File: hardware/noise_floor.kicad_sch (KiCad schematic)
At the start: 15 parts, among them J1 DC Power, J10 IO/Switch Connector 2 (Switch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, J2 Input, J3 Output, J4 Battery Negative (optional), J5 Battery Positive (optional), J6 IO/Effect Connector 1 (IO Sid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, J7 IO/Switch Connector 1 (IO Sid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, J8 IO/Switch Connector 2 (IO Sid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, J9 IO/Switch Connector 1 (Switch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, SW1 Footswitch

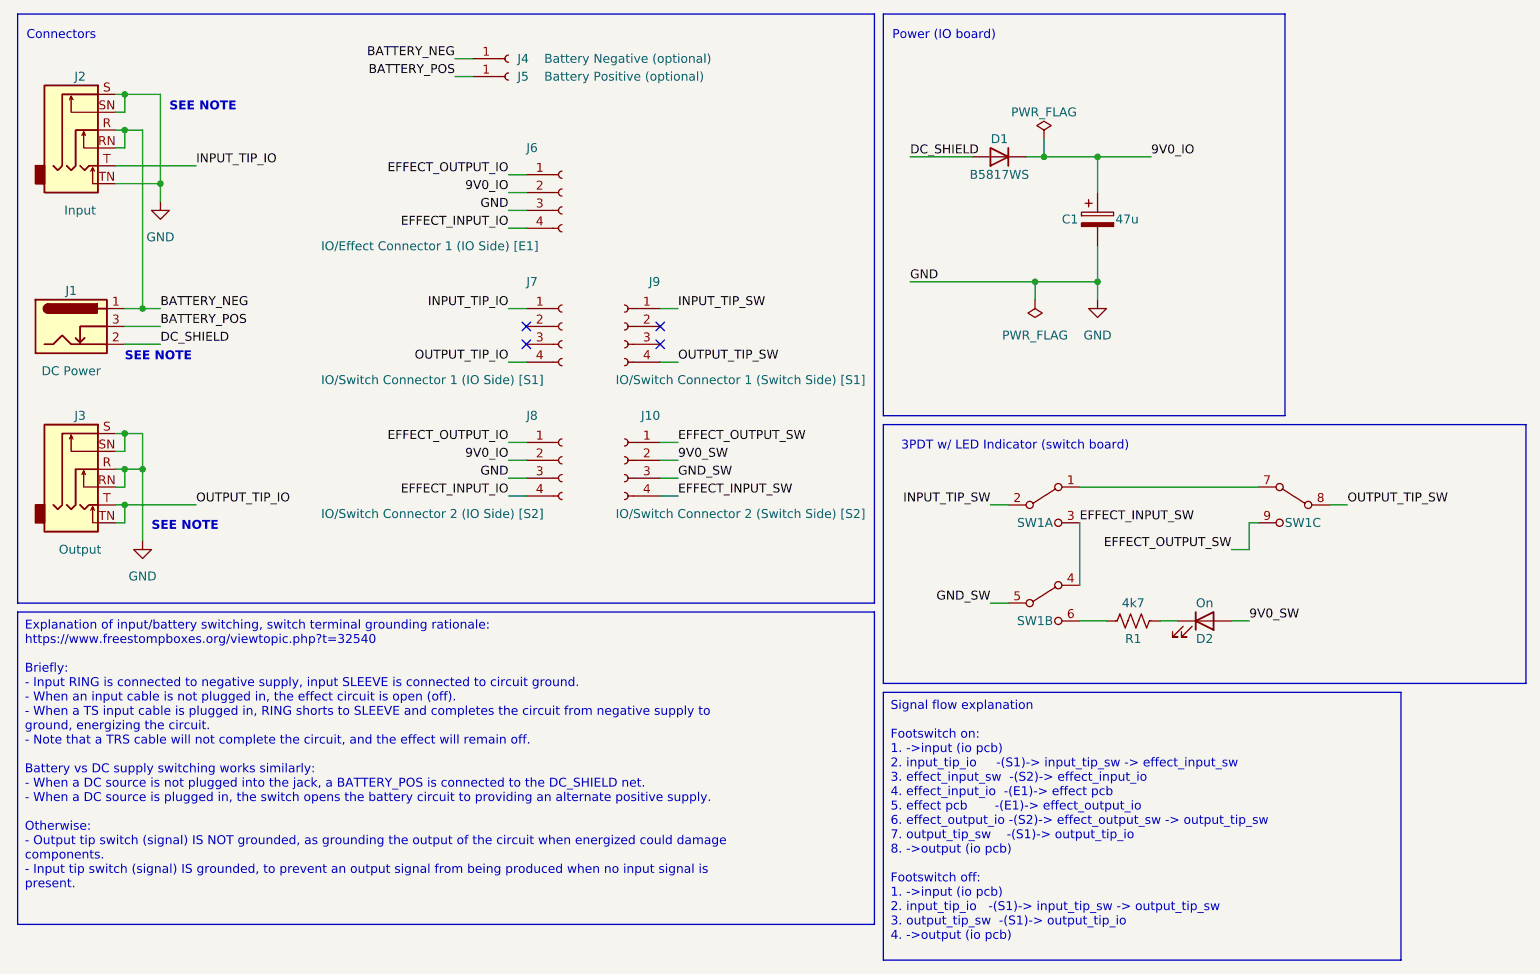
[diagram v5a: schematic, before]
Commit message: slight adjustment to input switch behavior, add note about chassis ground
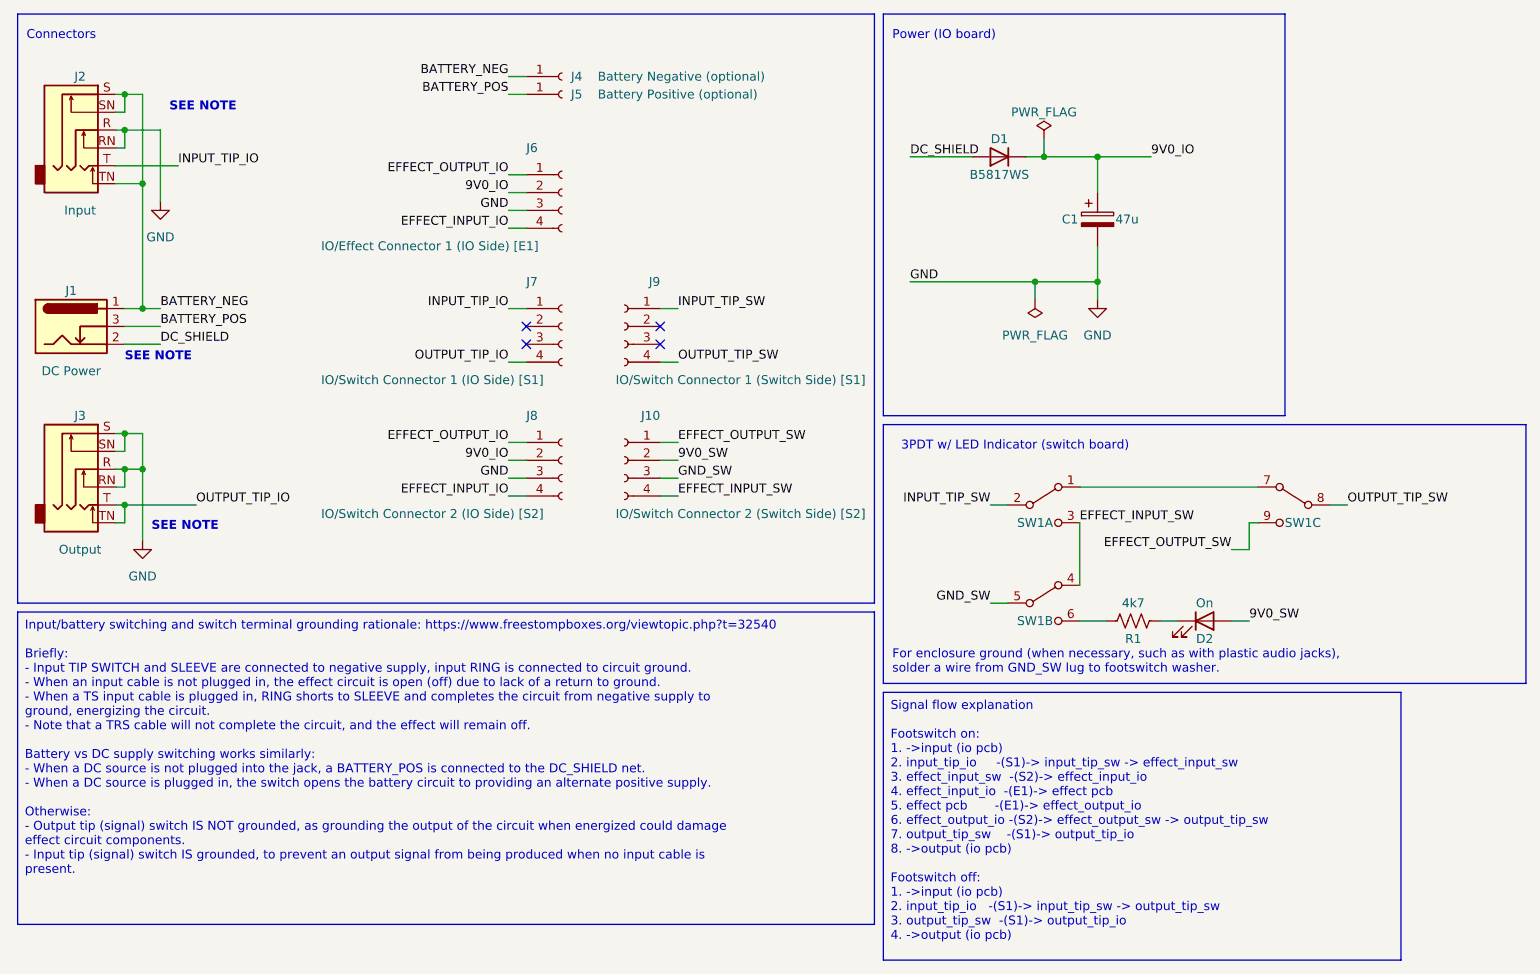
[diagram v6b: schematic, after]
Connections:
- net BATTERY_NEG: now also J2.S, J2.SN, J2.TN; no longer J2.R, J2.RN
- net GND: now also J2.R, J2.RN; no longer J2.S, J2.SN, J2.TN
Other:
- note added: "For enclosure ground (when necessary, such as with plastic audio jacks), solder a wire from GND_SW lug to footswitch washer."
- moved on the sheet: J4, J5

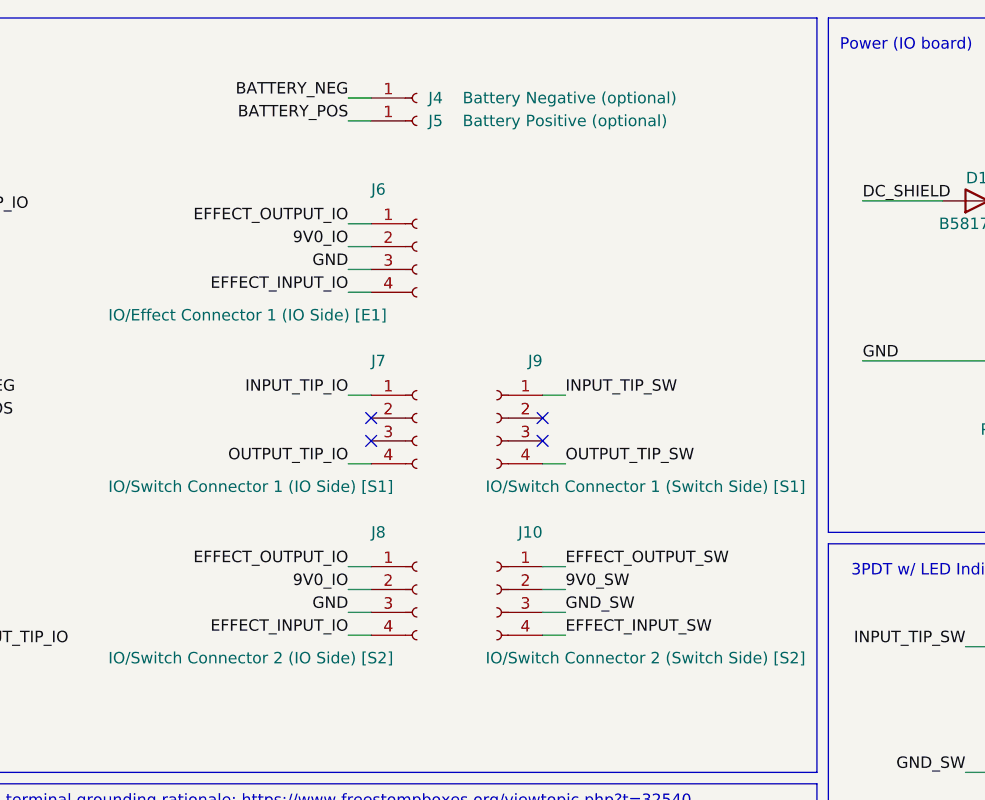
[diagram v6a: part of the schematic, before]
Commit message: Fix errata from v0.03 prototype inspection:
 - Switch to narrower amphenol phone jacks to better fit within 125B enclosure
 - Swap pin ordering for picoblade connections on IO board, as retail cable assemblies swap pin order
 -

Also:

 - Add JST XH header for battery connection

Another commit will complete the reroute shortly.
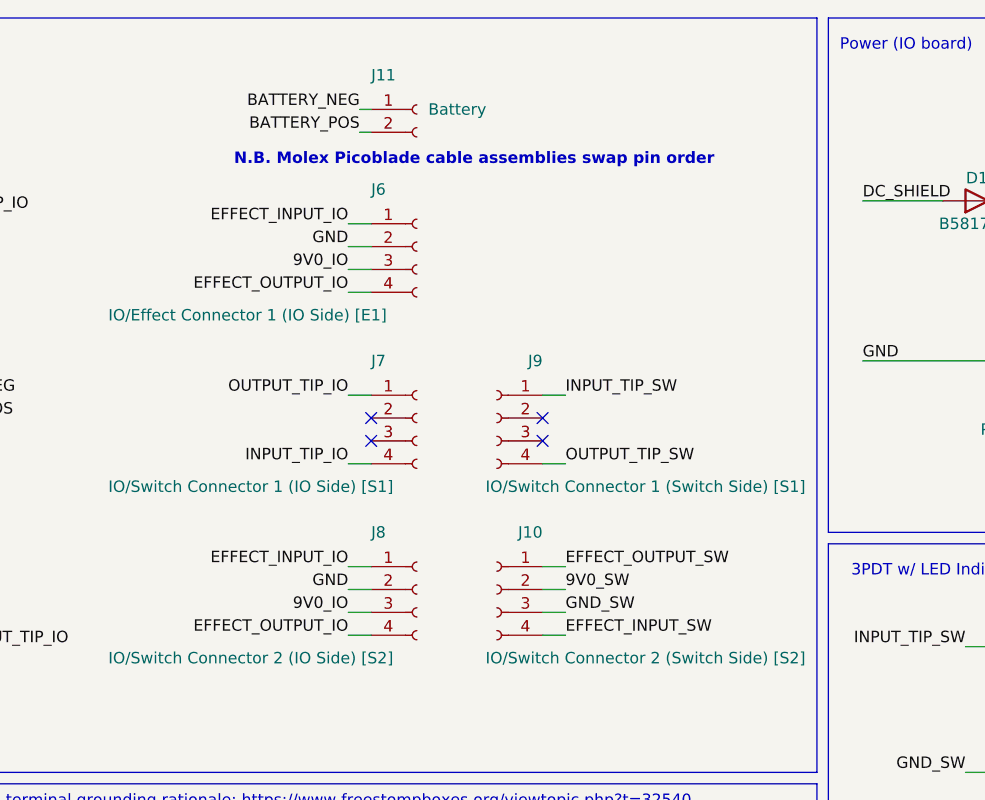
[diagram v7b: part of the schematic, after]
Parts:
- removed J4: Battery Negative (optional), Connector_Wire:SolderWire-0.25sqmm_1x01_D0.65mm_OD2mm, symbol Connector:Conn_01x01_Socket
- removed J5: Battery Positive (optional), Connector_Wire:SolderWire-0.25sqmm_1x01_D0.65mm_OD2mm, symbol Connector:Conn_01x01_Socket
- added J11: Battery, Connector_JST:JST_XH_B2B-XH-A_1x02_P2.50mm_Vertical, symbol Connector:Conn_01x02_Socket
- J2, J3: footprint noise_floor:Jack_6.35mm_Neutrik_NMJ6HCD2_Horizontal-3DModel_from_Vasily_Kashirin -> noise_floor:ACJS-MHOM
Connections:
- net 9V0_IO: now also J6.3 (Pin_3), J8.3 (Pin_3); no longer J6.2 (Pin_2), J8.2 (Pin_2)
- net BATTERY_NEG: now also J11.1 (Pin_1)
- net BATTERY_POS: now also J11.2 (Pin_2)
- net EFFECT_INPUT_IO: now also J6.1 (Pin_1), J8.1 (Pin_1); no longer J6.4 (Pin_4), J8.4 (Pin_4)
- net EFFECT_OUTPUT_IO: now also J6.4 (Pin_4), J8.4 (Pin_4); no longer J6.1 (Pin_1), J8.1 (Pin_1)
- net GND: now also J6.2 (Pin_2), J8.2 (Pin_2); no longer J6.3 (Pin_3), J8.3 (Pin_3)
- net INPUT_TIP_IO: now also J7.4 (Pin_4); no longer J7.1 (Pin_1)
- net OUTPUT_TIP_IO: now also J7.1 (Pin_1); no longer J7.4 (Pin_4)
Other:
- note added: "N.B. Molex Picoblade cable assemblies swap pin order"
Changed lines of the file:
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@@
   (title_block
     (title "Noise Floor Interface Boards")
-    (date "2023-03-04")
-    (rev "v0.07")
+    (date "2023-03-10")
+    (rev "v0.1")
     (comment 1 "github.com/whbeers/noise_floor")
   )
@@
     (stroke (width 0) (type default))
   )
-  (wire (pts (xy 83.82 22.86) (xy 86.36 22.86))
+  (wire (pts (xy 85.09 24.13) (xy 86.36 24.13))
     (stroke (width 0) (type default))
   )
@@
     (stroke (width 0) (type default))
   )
-  (wire (pts (xy 83.82 25.4) (xy 86.36 25.4))
-    (stroke (width 0) (type default))
-  )
   (wire (pts (xy 83.82 63.5) (xy 86.36 63.5))
     (stroke (width 0) (type default))
@@
   )
   (wire (pts (xy 27.94 35.56) (xy 36.83 35.56))
+    (stroke (width 0) (type default))
+  )
+  (wire (pts (xy 85.09 26.67) (xy 86.36 26.67))
     (stroke (width 0) (type default))
   )
@@
     (effects (font (size 1.27 1.27) (thickness 0.254) bold (color 255 0 0 1)) (justify left bottom))
   )
+  (text "N.B. Molex Picoblade cable assemblies swap pin order"
+    (at 71.12 30.48 0)
+    (effects (font (size 1.27 1.27) (thickness 0.254) bold (color 255 0 0 1)) (justify left bottom))
+  )
   (label "GND" (at 140.97 52.07 0) (fields_autoplaced)
     (effects (font (size 1.27 1.27)) (justify left bottom))
@@
     (effects (font (size 1.27 1.27)) (justify left bottom))
   )
-  (label "BATTERY_POS" (at 83.82 25.4 180) (fields_autoplaced)
-    (effects (font (size 1.27 1.27)) (justify right bottom))
-  )
-  (label "BATTERY_NEG" (at 83.82 22.86 180) (fields_autoplaced)
+  (label "BATTERY_POS" (at 85.09 26.67 180) (fields_autoplaced)
+    (effects (font (size 1.27 1.27)) (justify right bottom))
+  )
+  (label "BATTERY_NEG" (at 85.09 24.13 180) (fields_autoplaced)
     (effects (font (size 1.27 1.27)) (justify right bottom))
   )
@@
     (effects (font (size 1.27 1.27)) (justify left bottom))
   )
-  (label "EFFECT_INPUT_IO" (at 83.82 82.55 180) (fields_autoplaced)
-    (effects (font (size 1.27 1.27)) (justify right bottom))
-  )
-  (label "EFFECT_INPUT_IO" (at 83.82 44.45 180) (fields_autoplaced)
+  (label "EFFECT_OUTPUT_IO" (at 83.82 82.55 180) (fields_autoplaced)
+    (effects (font (size 1.27 1.27)) (justify right bottom))
+  )
+  (label "EFFECT_OUTPUT_IO" (at 83.82 44.45 180) (fields_autoplaced)
     (effects (font (size 1.27 1.27)) (justify right bottom))
   )
@@
     (effects (font (size 1.27 1.27)) (justify left bottom))
   )
-  (label "9V0_IO" (at 83.82 39.37 180) (fields_autoplaced)
+  (label "GND" (at 83.82 39.37 180) (fields_autoplaced)
     (effects (font (size 1.27 1.27)) (justify right bottom))
   )
@@
     (effects (font (size 1.27 1.27)) (justify right bottom))
   )
-  (label "GND" (at 83.82 80.01 180) (fields_autoplaced)
-    (effects (font (size 1.27 1.27)) (justify right bottom))
-  )
-  (label "EFFECT_OUTPUT_IO" (at 83.82 36.83 180) (fields_autoplaced)
+  (label "9V0_IO" (at 83.82 80.01 180) (fields_autoplaced)
+    (effects (font (size 1.27 1.27)) (justify right bottom))
+  )
+  (label "EFFECT_INPUT_IO" (at 83.82 36.83 180) (fields_autoplaced)
     (effects (font (size 1.27 1.27)) (justify right bottom))
   )
@@
     (effects (font (size 1.27 1.27)) (justify right bottom))
   )
-  (label "INPUT_TIP_IO" (at 83.82 55.88 180)
-    (effects (font (size 1.27 1.27)) (justify right bottom))
-    (property "Label" "In_Left" (at 97.79 55.88 0)
-      (effects (font (size 1.27 1.27) italic) (justify right) hide)
-    )
+  (label "OUTPUT_TIP_IO" (at 83.82 55.88 180)
+    (effects (font (size 1.27 1.27)) (justify right bottom))
   )
   (label "OUTPUT_TIP_SW" (at 203.2 83.82 0) (fields_autoplaced)
     (effects (font (size 1.27 1.27)) (justify left bottom))
   )
-  (label "9V0_IO" (at 83.82 77.47 180) (fields_autoplaced)
-    (effects (font (size 1.27 1.27)) (justify right bottom))
-  )
-  (label "GND" (at 83.82 41.91 180) (fields_autoplaced)
+  (label "GND" (at 83.82 77.47 180) (fields_autoplaced)
+    (effects (font (size 1.27 1.27)) (justify right bottom))
+  )
+  (label "9V0_IO" (at 83.82 41.91 180) (fields_autoplaced)
     (effects (font (size 1.27 1.27)) (justify right bottom))
   )
@@
     (effects (font (size 1.27 1.27)) (justify left bottom))
   )
-  (label "EFFECT_OUTPUT_IO" (at 83.82 74.93 180) (fields_autoplaced)
+  (label "EFFECT_INPUT_IO" (at 83.82 74.93 180) (fields_autoplaced)
     (effects (font (size 1.27 1.27)) (justify right bottom))
   )
@@
     (effects (font (size 1.27 1.27)) (justify left bottom))
   )
-  (label "OUTPUT_TIP_IO" (at 83.82 63.5 180) (fields_autoplaced)
+  (label "INPUT_TIP_IO" (at 83.82 63.5 180) (fields_autoplaced)
     (effects (font (size 1.27 1.27)) (justify right bottom))
   )
@@
     (effects (font (size 1.27 1.27)) (justify left bottom))
   )
-  (symbol (lib_id "Connector:Conn_01x01_Socket") (at 91.44 25.4 0) (unit 1)
-    (in_bom yes) (on_board yes) (dnp no)
-    (property "Reference" "J5" (at 92.71 25.4 0)
-      (effects (font (size 1.27 1.27)) (justify left))
-    )
-    (property "Value" "Battery Positive (optional)" (at 96.52 25.4 0)
-      (effects (font (size 1.27 1.27)) (justify left))
-    )
-    (property "Footprint" "Connector_Wire:SolderWire-0.25sqmm_1x01_D0.65mm_OD2mm" (at 91.44 25.4 0)
-      (effects (font (size 1.27 1.27)) hide)
-    )
-    (property "Datasheet" "~" (at 91.44 25.4 0)
-      (effects (font (size 1.27 1.27)) hide)
-    )
-    (pin "1")
-    (instances
-      (project "noise_floor"
-        (path "/f19766fa-80fa-493c-bad9-ad922f69593a"
-          (reference "J5") (unit 1)
+  (symbol (lib_id "Connector:Conn_01x02_Socket") (at 91.44 24.13 0) (unit 1)
+    (in_bom yes) (on_board yes) (dnp no)
+    (property "Reference" "J11" (at 86.36 20.32 0)
+      (effects (font (size 1.27 1.27)) (justify left))
+    )
+    (property "Value" "Battery" (at 92.71 24.13 0)
+      (effects (font (size 1.27 1.27)) (justify left))
+    )
+    (property "Footprint" "Connector_JST:JST_XH_B2B-XH-A_1x02_P2.50mm_Vertical" (at 91.44 24.13 0)
+      (effects (font (size 1.27 1.27)) hide)
+    )
+    (property "Datasheet" "~" (at 91.44 24.13 0)
+      (effects (font (size 1.27 1.27)) hide)
+    )
+    (pin "1")
+    (pin "2")
+    (instances
+      (project "noise_floor"
+        (path "/f19766fa-80fa-493c-bad9-ad922f69593a"
+          (reference "J11") (unit 1)
         )
       )
@@
       (effects (font (size 1.27 1.27)))
     )
-    (property "Footprint" "noise_floor:Jack_6.35mm_Neutrik_NMJ6HCD2_Horizontal-3DModel_from_Vasily_Kashirin" (at 22.86 78.74 0)
+    (property "Footprint" "noise_floor:ACJS-MHOM" (at 22.86 78.74 0)
       (effects (font (size 1.27 1.27)) hide)
     )
@@
     )
   )
-  (symbol (lib_id "Connector:Conn_01x01_Socket") (at 91.44 22.86 0) (unit 1)
-    (in_bom yes) (on_board yes) (dnp no)
-    (property "Reference" "J4" (at 92.71 22.86 0)
-      (effects (font (size 1.27 1.27)) (justify left))
-    )
-    (property "Value" "Battery Negative (optional)" (at 96.52 22.86 0)
-      (effects (font (size 1.27 1.27)) (justify left))
-    )
-    (property "Footprint" "Connector_Wire:SolderWire-0.25sqmm_1x01_D0.65mm_OD2mm" (at 91.44 22.86 0)
-      (effects (font (size 1.27 1.27)) hide)
-    )
-    (property "Datasheet" "~" (at 91.44 22.86 0)
-      (effects (font (size 1.27 1.27)) hide)
-    )
-    (pin "1")
-    (instances
-      (project "noise_floor"
-        (path "/f19766fa-80fa-493c-bad9-ad922f69593a"
-          (reference "J4") (unit 1)
-        )
-      )
-    )
-  )
   (symbol (lib_id "Connector_Audio:AudioJack3_Switch") (at 22.86 30.48 0) (unit 1)
     (in_bom yes) (on_board yes) (dnp no)
@@
       (effects (font (size 1.27 1.27)))
     )
-    (property "Footprint" "noise_floor:Jack_6.35mm_Neutrik_NMJ6HCD2_Horizontal-3DModel_from_Vasily_Kashirin" (at 22.86 30.48 0)
-      (effects (font (size 1.27 1.27)) hide)
-    )
+    (property "Footprint" "noise_floor:ACJS-MHOM" (at 22.86 30.48 0)
+      (effects (font (size 1.27 1.27)) hide)
+    )
